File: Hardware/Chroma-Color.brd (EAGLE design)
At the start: 106.4 x 50.5 mm, 92 parts, among them J1 15-91-1102, J2 87832-6422, J3 1775470-6, J4 D2514-6V0C-AR-WD, J7 26-64-4040, U1 EP4CE6E22C8N, U2 ADP3338AKCZ-3.3-RL, U3 ADP3338AKCZ-2.5-RL, U4 NCV565ST12T3G, U5 M25P40-VMN6TPBCT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

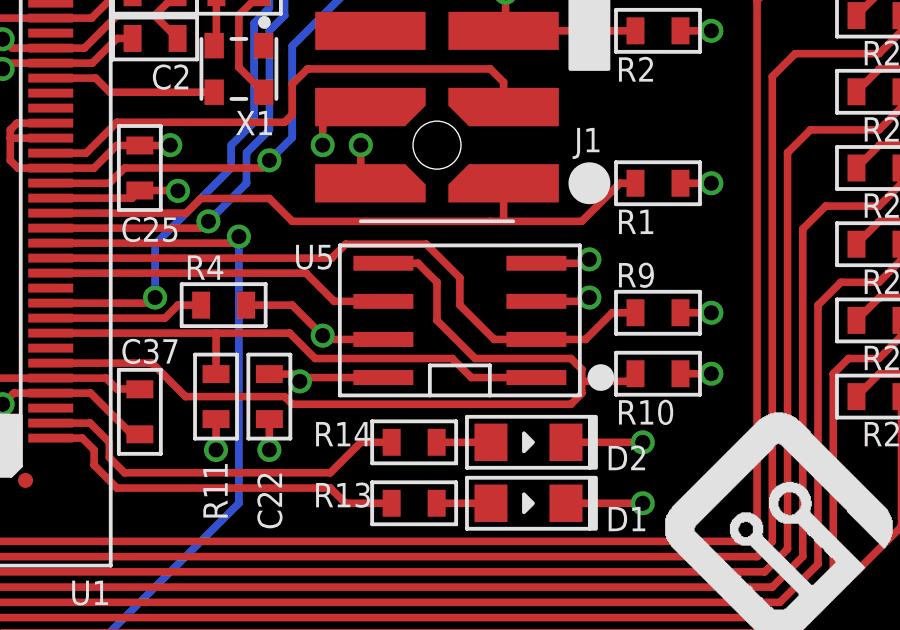
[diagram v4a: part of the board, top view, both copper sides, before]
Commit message: Updated to latest library style.
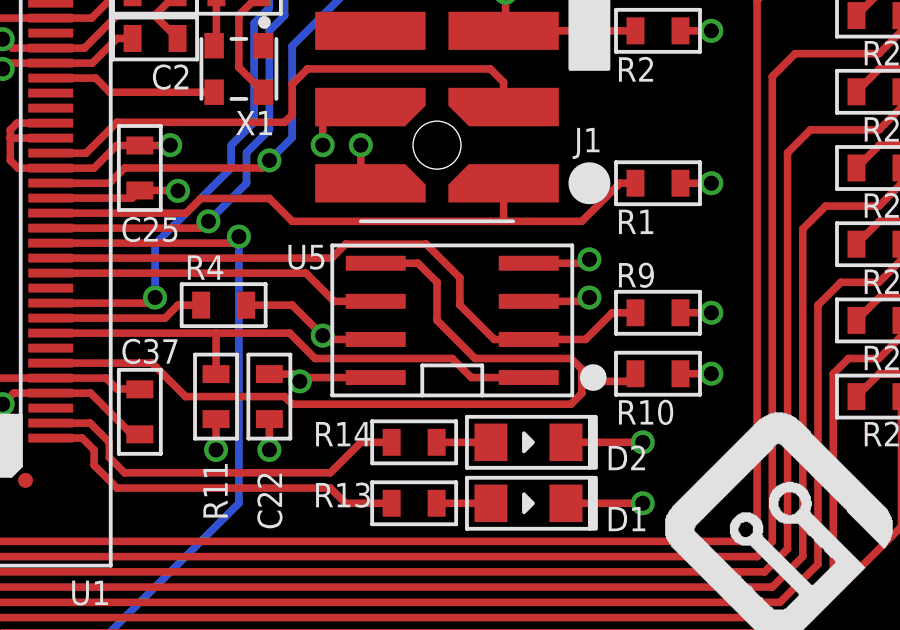
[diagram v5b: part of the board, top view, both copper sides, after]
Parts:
- U5: device PP_DigitalIC:SOIC-8 -> PP_DigitalIC:M25P40_SOIC-8
- moved U5 0.25 mm to (69.6, 13.0), turned to 180 degrees
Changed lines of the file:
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@@
 <element name="U3" library="PP_PowerIC" package="ADP3338_SOT-223-3" value="ADP3338AKCZ-2.5-RL" x="75.184" y="41.656"/>
 <element name="U4" library="PP_PowerIC" package="NCV565_SOT-223-3" value="NCV565ST12T3G" x="65.786" y="41.656"/>
-<element name="U5" library="PP_DigitalIC" package="SOIC-8" value="M25P40-VMN6TPBCT" x="69.85" y="12.954" smashed="yes" rot="R90">
-<attribute name="NAME" x="64.302" y="14.66" size="0.8128" layer="21" font="vector" ratio="16"/>
+<element name="U5" library="PP_DigitalIC" package="M25P40_SOIC-8" value="M25P40-VMN6TPBCT" x="69.596" y="12.954" smashed="yes" rot="R180">
+<attribute name="NAME" x="64.048" y="14.66" size="0.8128" layer="21" font="vector" ratio="16"/>
 </element>
 <element name="R9" library="MF_Passives" package="R0603" value="10K" x="76.454" y="13.208" smashed="yes" rot="R180">
@@
 <wire x1="12.192" y1="48.768" x2="12.192" y2="49.022" width="0.254" layer="2"/>
 <wire x1="68.326" y1="29.464" x2="68.326" y2="29.718" width="0.254" layer="2"/>
-<wire x1="72.4" y1="14.859" x2="74.041" y2="14.859" width="0.254" layer="1"/>
+<wire x1="72.146" y1="14.859" x2="74.041" y2="14.859" width="0.254" layer="1"/>
 <wire x1="74.041" y1="14.859" x2="74.168" y2="14.986" width="0.254" layer="1"/>
 <via x="74.168" y="14.986" extent="1-16" drill="0.5"/>
@@
 <via x="34.29" y="48.768" extent="1-16" drill="0.5"/>
 <wire x1="34.29" y1="48.768" x2="34.036" y2="49.022" width="0.254" layer="15"/>
-<wire x1="72.4" y1="13.589" x2="74.041" y2="13.589" width="0.254" layer="1"/>
+<wire x1="72.146" y1="13.589" x2="74.041" y2="13.589" width="0.254" layer="1"/>
 <wire x1="74.041" y1="13.589" x2="74.168" y2="13.716" width="0.254" layer="1"/>
 <via x="74.168" y="13.716" extent="1-16" drill="0.5"/>
 <wire x1="74.168" y1="13.716" x2="74.422" y2="13.97" width="0.254" layer="15"/>
-<wire x1="67.3" y1="11.049" x2="64.643" y2="11.049" width="0.254" layer="1"/>
+<wire x1="67.046" y1="11.049" x2="64.643" y2="11.049" width="0.254" layer="1"/>
 <wire x1="64.643" y1="11.049" x2="64.516" y2="10.922" width="0.254" layer="1"/>
 <via x="64.516" y="10.922" extent="1-16" drill="0.5"/>
-<wire x1="67.3" y1="12.319" x2="65.405" y2="12.319" width="0.254" layer="1"/>
+<wire x1="67.046" y1="12.319" x2="65.405" y2="12.319" width="0.254" layer="1"/>
 <wire x1="65.405" y1="12.319" x2="65.278" y2="12.446" width="0.254" layer="1"/>
 <via x="65.278" y="12.446" extent="1-16" drill="0.5"/>
@@
 <contactref element="R11" pad="P$2"/>
 <contactref element="U1" pad="8"/>
-<wire x1="72.4" y1="11.049" x2="70.231" y2="11.049" width="0.254" layer="1"/>
+<wire x1="72.146" y1="11.049" x2="70.231" y2="11.049" width="0.254" layer="1"/>
 <wire x1="70.231" y1="11.049" x2="69.596" y2="11.684" width="0.254" layer="1"/>
 <wire x1="64.178" y1="12.53" x2="61.722" y2="12.53" width="0.254" layer="1"/>
@@
 <contactref element="U5" pad="2"/>
 <contactref element="U1" pad="13"/>
-<wire x1="72.4" y1="12.319" x2="70.993" y2="12.319" width="0.254" layer="1"/>
+<wire x1="72.146" y1="12.319" x2="70.993" y2="12.319" width="0.254" layer="1"/>
 <wire x1="70.993" y1="12.319" x2="69.85" y2="13.462" width="0.254" layer="1"/>
 <wire x1="69.85" y1="13.462" x2="69.85" y2="14.375609375" width="0.254" layer="1"/>
@@
 <wire x1="66.04" y1="15.494" x2="65.576" y2="15.03" width="0.254" layer="1"/>
 <wire x1="65.576" y1="15.03" x2="56.212" y2="15.03" width="0.254" layer="1"/>
-<wire x1="72.4" y1="12.319" x2="74.041" y2="12.319" width="0.254" layer="1"/>
+<wire x1="72.146" y1="12.319" x2="74.041" y2="12.319" width="0.254" layer="1"/>
 <wire x1="74.041" y1="12.319" x2="74.93" y2="13.208" width="0.254" layer="1"/>
 <wire x1="74.93" y1="13.208" x2="75.704" y2="13.208" width="0.254" layer="1"/>
@@
 <contactref element="R10" pad="P$2"/>
 <contactref element="U1" pad="6"/>
-<wire x1="67.3" y1="14.859" x2="68.453" y2="14.859" width="0.254" layer="1"/>
+<wire x1="67.046" y1="14.859" x2="68.453" y2="14.859" width="0.254" layer="1"/>
 <wire x1="68.453" y1="14.859" x2="69.088" y2="14.224" width="0.254" layer="1"/>
 <wire x1="69.088" y1="14.224" x2="69.088" y2="12.954" width="0.254" layer="1"/>
@@
 <contactref element="U5" pad="6"/>
 <contactref element="U1" pad="12"/>
-<wire x1="67.3" y1="13.589" x2="65.659" y2="13.589" width="0.254" layer="1"/>
+<wire x1="67.046" y1="13.589" x2="65.659" y2="13.589" width="0.254" layer="1"/>
 <wire x1="65.659" y1="13.589" x2="64.718" y2="14.53" width="0.254" layer="1"/>
 <wire x1="56.212" y1="14.53" x2="64.718" y2="14.53" width="0.254" layer="1"/>
